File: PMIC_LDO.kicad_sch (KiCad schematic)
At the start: 20 parts, among them U5 RK809-2

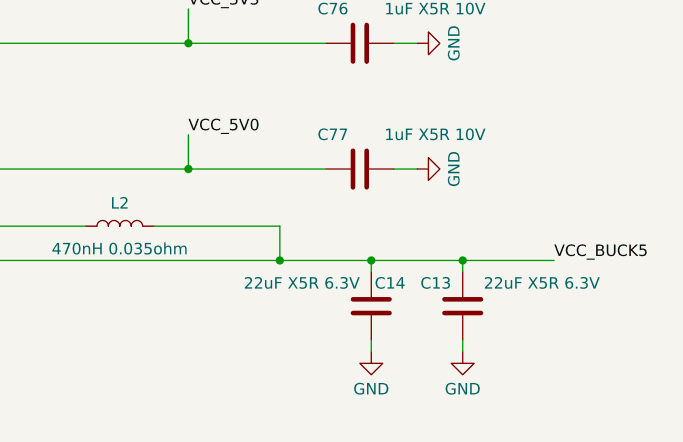
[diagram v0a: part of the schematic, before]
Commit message: updated LCSC selection of capacitors
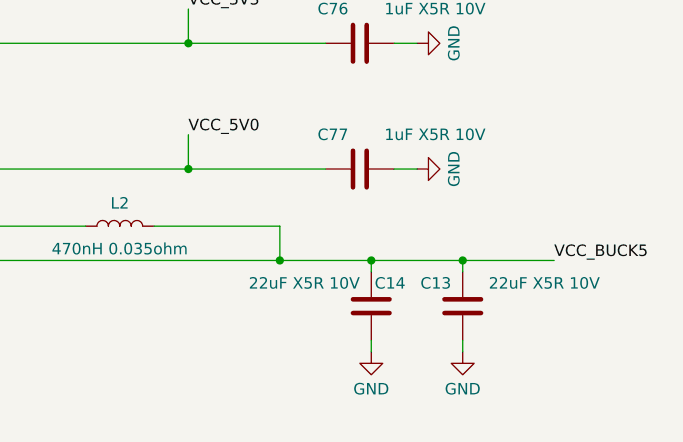
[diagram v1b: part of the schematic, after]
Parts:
- C13, C14: value 22uF X5R 6.3V -> 22uF X5R 10V; LCSC (none) -> C162690; Model (none) -> ZRB18AR61A226ME01L; Vendor (none) -> muRata(村田)
- C66: footprint Capacitor_SMD:C_0603_1608Metric -> Capacitor_SMD:C_0402_1005Metric; LCSC C469532 -> C77000; Model GRM188B31A106KE69D -> GRM155R61A106ME44D
- C67, C68, C69, C71, C72, C73, C74, C75, C76, C77: LCSC (none) -> C77007; Model (none) -> GRM155R61C105KE01D; Vendor (none) -> muRata(村田)
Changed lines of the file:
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@@
+      (effects (font (size 1.27 1.27)) hide)
+    )
+    (property "Description" "容值: 1uF 精度: ±10% 额定电压: 16V 材质(温度系数): X5R 材质:X5R" (at 209.55 118.11 0)
+      (effects (font (size 1.27 1.27)) hide)
+    )
+    (property "LCSC" "C77007" (at 209.55 118.11 0)
+      (effects (font (size 1.27 1.27)) hide)
+    )
+    (property "Model" "GRM155R61C105KE01D" (at 209.55 118.11 0)
+      (effects (font (size 1.27 1.27)) hide)
+    )
+    (property "Vendor" "muRata(村田)" (at 209.55 118.11 0)
       (effects (font (size 1.27 1.27)) hide)
     )
@@
       (effects (font (size 1.27 1.27)) hide)
     )
+    (property "Description" "容值: 1uF 精度: ±10% 额定电压: 16V 材质(温度系数): X5R 材质:X5R" (at 209.55 87.63 0)
+      (effects (font (size 1.27 1.27)) hide)
+    )
+    (property "LCSC" "C77007" (at 209.55 87.63 0)
+      (effects (font (size 1.27 1.27)) hide)
+    )
+    (property "Model" "GRM155R61C105KE01D" (at 209.55 87.63 0)
+      (effects (font (size 1.27 1.27)) hide)
+    )
+    (property "Vendor" "muRata(村田)" (at 209.55 87.63 0)
+      (effects (font (size 1.27 1.27)) hide)
+    )
     (pin "1")
     (pin "2")
@@
       (effects (font (size 1.27 1.27)) hide)
     )
+    (property "Description" "容值: 1uF 精度: ±10% 额定电压: 16V 材质(温度系数): X5R 材质:X5R" (at 209.55 45.72 0)
+      (effects (font (size 1.27 1.27)) hide)
+    )
+    (property "LCSC" "C77007" (at 209.55 45.72 0)
+      (effects (font (size 1.27 1.27)) hide)
+    )
+    (property "Model" "GRM155R61C105KE01D" (at 209.55 45.72 0)
+      (effects (font (size 1.27 1.27)) hide)
+    )
+    (property "Vendor" "muRata(村田)" (at 209.55 45.72 0)
+      (effects (font (size 1.27 1.27)) hide)
+    )
     (pin "1")
     (pin "2")
@@
     )
     (property "Datasheet" "~" (at 209.55 36.83 0)
+      (effects (font (size 1.27 1.27)) hide)
+    )
+    (property "Description" "容值: 1uF 精度: ±10% 额定电压: 16V 材质(温度系数): X5R 材质:X5R" (at 209.55 36.83 0)
+      (effects (font (size 1.27 1.27)) hide)
+    )
+    (property "LCSC" "C77007" (at 209.55 36.83 0)
+      (effects (font (size 1.27 1.27)) hide)
+    )
+    (property "Model" "GRM155R61C105KE01D" (at 209.55 36.83 0)
+      (effects (font (size 1.27 1.27)) hide)
+    )
+    (property "Vendor" "muRata(村田)" (at 209.55 36.83 0)
       (effects (font (size 1.27 1.27)) hide)
     )
@@
       (effects (font (size 1.27 1.27)) hide)
     )
+    (property "Description" "容值: 1uF 精度: ±10% 额定电压: 16V 材质(温度系数): X5R 材质:X5R" (at 209.55 29.21 0)
+      (effects (font (size 1.27 1.27)) hide)
+    )
+    (property "LCSC" "C77007" (at 209.55 29.21 0)
+      (effects (font (size 1.27 1.27)) hide)
+    )
+    (property "Model" "GRM155R61C105KE01D" (at 209.55 29.21 0)
+      (effects (font (size 1.27 1.27)) hide)
+    )
+    (property "Vendor" "muRata(村田)" (at 209.55 29.21 0)
+      (effects (font (size 1.27 1.27)) hide)
+    )
     (pin "1")
     (pin "2")
@@
       (effects (font (size 1.27 1.27)) (justify left))
     )
-    (property "Value" "22uF X5R 6.3V" (at 236.22 144.78 0)
+    (property "Value" "22uF X5R 10V" (at 236.22 144.78 0)
       (effects (font (size 1.27 1.27)) (justify left))
     )
@@
     )
     (property "Datasheet" "~" (at 220.98 147.32 0)
+      (effects (font (size 1.27 1.27)) hide)
+    )
+    (property "Description" "容值: 22uF 精度: ±20% 额定电压: 10V 材质(温度系数): X5R 材质：X5R" (at 220.98 147.32 0)
+      (effects (font (size 1.27 1.27)) hide)
+    )
+    (property "LCSC" "C162690" (at 220.98 147.32 0)
+      (effects (font (size 1.27 1.27)) hide)
+    )
+    (property "Model" "ZRB18AR61A226ME01L" (at 220.98 147.32 0)
+      (effects (font (size 1.27 1.27)) hide)
+    )
+    (property "Vendor" "muRata(村田)" (at 220.98 147.32 0)
       (effects (font (size 1.27 1.27)) hide)
     )
@@
       (effects (font (size 1.27 1.27)) hide)
     )
+    (property "Description" "容值: 1uF 精度: ±10% 额定电压: 16V 材质(温度系数): X5R 材质:X5R" (at 209.55 67.31 0)
+      (effects (font (size 1.27 1.27)) hide)
+    )
+    (property "LCSC" "C77007" (at 209.55 67.31 0)
+      (effects (font (size 1.27 1.27)) hide)
+    )
+    (property "Model" "GRM155R61C105KE01D" (at 209.55 67.31 0)
+      (effects (font (size 1.27 1.27)) hide)
+    )
+    (property "Vendor" "muRata(村田)" (at 209.55 67.31 0)
+      (effects (font (size 1.27 1.27)) hide)
+    )
     (pin "1")
     (pin "2")
@@
       (effects (font (size 1.27 1.27)) hide)
     )
+    (property "Description" "容值: 1uF 精度: ±10% 额定电压: 16V 材质(温度系数): X5R 材质:X5R" (at 209.55 105.41 0)
+      (effects (font (size 1.27 1.27)) hide)
+    )
+    (property "LCSC" "C77007" (at 209.55 105.41 0)
+      (effects (font (size 1.27 1.27)) hide)
+    )
+    (property "Model" "GRM155R61C105KE01D" (at 209.55 105.41 0)
+      (effects (font (size 1.27 1.27)) hide)
+    )
+    (property "Vendor" "muRata(村田)" (at 209.55 105.41 0)
+      (effects (font (size 1.27 1.27)) hide)
+    )
     (pin "1")
     (pin "2")
@@
     )
     (property "Datasheet" "~" (at 209.55 96.52 0)
+      (effects (font (size 1.27 1.27)) hide)
+    )
+    (property "Description" "容值: 1uF 精度: ±10% 额定电压: 16V 材质(温度系数): X5R 材质:X5R" (at 209.55 96.52 0)
+      (effects (font (size 1.27 1.27)) hide)
+    )
+    (property "LCSC" "C77007" (at 209.55 96.52 0)
+      (effects (font (size 1.27 1.27)) hide)
+    )
+    (property "Model" "GRM155R61C105KE01D" (at 209.55 96.52 0)
+      (effects (font (size 1.27 1.27)) hide)
+    )
+    (property "Vendor" "muRata(村田)" (at 209.55 96.52 0)
       (effects (font (size 1.27 1.27)) hide)
     )
@@
       (effects (font (size 1.27 1.27)) hide)
     )
+    (property "Description" "容值: 1uF 精度: ±10% 额定电压: 16V 材质(温度系数): X5R 材质:X5R" (at 209.55 76.2 0)
+      (effects (font (size 1.27 1.27)) hide)
+    )
+    (property "LCSC" "C77007" (at 209.55 76.2 0)
+      (effects (font (size 1.27 1.27)) hide)
+    )
+    (property "Model" "GRM155R61C105KE01D" (at 209.55 76.2 0)
+      (effects (font (size 1.27 1.27)) hide)
+    )
+    (property "Vendor" "muRata(村田)" (at 209.55 76.2 0)
+      (effects (font (size 1.27 1.27)) hide)
+    )
     (pin "1")
     (pin "2")
@@
       (effects (font (size 1.27 1.27)) hide)
     )
+    (property "Description" "容值: 1uF 精度: ±10% 额定电压: 16V 材质(温度系数): X5R 材质:X5R" (at 209.55 132.08 0)
+      (effects (font (size 1.27 1.27)) hide)
+    )
+    (property "LCSC" "C77007" (at 209.55 132.08 0)
+      (effects (font (size 1.27 1.27)) hide)
+    )
+    (property "Model" "GRM155R61C105KE01D" (at 209.55 132.08 0)
+      (effects (font (size 1.27 1.27)) hide)
+    )
+    (property "Vendor" "muRata(村田)" (at 209.55 132.08 0)
+      (effects (font (size 1.27 1.27)) hide)
+    )
     (pin "1")
     (pin "2")
@@
       (effects (font (size 1.27 1.27)) (justify left))
     )
-    (property "Value" "22uF X5R 6.3V" (at 209.55 144.78 0)
+    (property "Value" "22uF X5R 10V" (at 209.55 144.78 0)
       (effects (font (size 1.27 1.27)) (justify left))
     )
@@
     )
     (property "Datasheet" "~" (at 210.82 147.32 0)
+      (effects (font (size 1.27 1.27)) hide)
+    )
+    (property "Description" "容值: 22uF 精度: ±20% 额定电压: 10V 材质(温度系数): X5R 材质：X5R" (at 210.82 147.32 0)
+      (effects (font (size 1.27 1.27)) hide)
+    )
+    (property "LCSC" "C162690" (at 210.82 147.32 0)
+      (effects (font (size 1.27 1.27)) hide)
+    )
+    (property "Model" "ZRB18AR61A226ME01L" (at 210.82 147.32 0)
+      (effects (font (size 1.27 1.27)) hide)
+    )
+    (property "Vendor" "muRata(村田)" (at 210.82 147.32 0)
       (effects (font (size 1.27 1.27)) hide)
     )
@@
       (effects (font (size 1.27 1.27)) (justify left))
     )
-    (property "Footprint" "Capacitor_SMD:C_0603_1608Metric" (at 111.4552 152.4 0)
+    (property "Footprint" "Capacitor_SMD:C_0402_1005Metric" (at 111.4552 152.4 0)
       (effects (font (size 1.27 1.27)) hide)
     )
@@
       (effects (font (size 1.27 1.27)) hide)
     )
-    (property "Description" "容值: 10uF 精度: ±10% 额定电压: 10V 材质(温度系数): B B(JIS)" (at 110.49 148.59 0)
-      (effects (font (size 1.27 1.27)) hide)
-    )
-    (property "LCSC" "C469532" (at 110.49 148.59 0)
-      (effects (font (size 1.27 1.27)) hide)
-    )
-    (property "Model" "GRM188B31A106KE69D" (at 110.49 148.59 0)
-      (effects (font (size 1.27 1.27)) hide)
-    )
+    (property "Description" "容值: 10uF 精度: ±20% 额定电压: 10V 材质(温度系数): X5R 材质:X5R" (at 110.49 148.59 0)
+      (effects (font (size 1.27 1.27)) hide)
+    )
+    (property "LCSC" "C77000" (at 110.49 148.59 0)
+      (effects (font (size 1.27 1.27)) hide)
+    )
+    (property "Model" "GRM155R61A106ME44D" (at 110.49 148.59 0)
+      (effects (font (size 1.27 1.27)) hide)
+    )

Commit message: updated foorprints
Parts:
- L2: value 470nH 0.035ohm -> 470nH 4.53A 0.035ohm; footprint (none) -> Inductor_SMD:L_1008_2520Metric; LCSC (none) -> C88530; Model (none) -> VLS252010HBX-R47M-1; Vendor (none) -> TDK
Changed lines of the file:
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@@
       (effects (font (size 1.27 1.27)))
     )
-    (property "Value" "470nH 0.035ohm" (at 182.88 140.97 90)
+    (property "Value" "470nH 4.53A 0.035ohm" (at 182.88 140.97 90)
       (effects (font (size 1.27 1.27)))
     )
-    (property "Footprint" "" (at 182.88 138.43 0)
+    (property "Footprint" "Inductor_SMD:L_1008_2520Metric" (at 182.88 138.43 0)
       (effects (font (size 1.27 1.27)) hide)
     )
@@
       (effects (font (size 1.27 1.27)) hide)
     )
+    (property "Description" "电感值: 470nH 精度: ±20% 额定电流: 3.32A 饱和电流(Isat): 4.53A 直流电阻(DCR): 35mΩ Q值: - 自谐振频率: - 车" (at 182.88 138.43 0)
+      (effects (font (size 1.27 1.27)) hide)
+    )
+    (property "LCSC" "C88530" (at 182.88 138.43 0)
+      (effects (font (size 1.27 1.27)) hide)
+    )
+    (property "Model" "VLS252010HBX-R47M-1" (at 182.88 138.43 0)
+      (effects (font (size 1.27 1.27)) hide)
+    )
+    (property "Vendor" "TDK" (at 182.88 138.43 0)
+      (effects (font (size 1.27 1.27)) hide)
+    )

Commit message: layout SoC Power and DDR capacitors
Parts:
- C62, C63, C64, C65: footprint Capacitor_SMD:C_0201_0603Metric -> Capacitor_SMD:C_0402_1005Metric; LCSC C76929 -> C15684; Model GRM033R60J105KEA2D -> GRM155R60J105KE19D
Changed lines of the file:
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@@
       (effects (font (size 1.27 1.27)) (justify left))
     )
-    (property "Footprint" "Capacitor_SMD:C_0201_0603Metric" (at 111.4552 127 0)
+    (property "Footprint" "Capacitor_SMD:C_0402_1005Metric" (at 111.4552 127 0)
       (effects (font (size 1.27 1.27)) hide)
     )
@@
       (effects (font (size 1.27 1.27)) hide)
     )
-    (property "LCSC" "C76929" (at 110.49 123.19 0)
-      (effects (font (size 1.27 1.27)) hide)
-    )
-    (property "Model" "GRM033R60J105KEA2D" (at 110.49 123.19 0)
+    (property "LCSC" "C15684" (at 110.49 123.19 0)
+      (effects (font (size 1.27 1.27)) hide)
+    )
+    (property "Model" "GRM155R60J105KE19D" (at 110.49 123.19 0)
       (effects (font (size 1.27 1.27)) hide)
     )
@@
       (effects (font (size 1.27 1.27)) (justify left))
     )
-    (property "Footprint" "Capacitor_SMD:C_0201_0603Metric" (at 111.4552 40.64 0)
+    (property "Footprint" "Capacitor_SMD:C_0402_1005Metric" (at 111.4552 40.64 0)
       (effects (font (size 1.27 1.27)) hide)
     )
@@
       (effects (font (size 1.27 1.27)) hide)
     )
-    (property "LCSC" "C76929" (at 110.49 36.83 0)
-      (effects (font (size 1.27 1.27)) hide)
-    )
-    (property "Model" "GRM033R60J105KEA2D" (at 110.49 36.83 0)
+    (property "LCSC" "C15684" (at 110.49 36.83 0)
+      (effects (font (size 1.27 1.27)) hide)
+    )
+    (property "Model" "GRM155R60J105KE19D" (at 110.49 36.83 0)
       (effects (font (size 1.27 1.27)) hide)
     )
@@
       (effects (font (size 1.27 1.27)) (justify left))
     )
-    (property "Footprint" "Capacitor_SMD:C_0201_0603Metric" (at 111.4552 68.58 0)
+    (property "Footprint" "Capacitor_SMD:C_0402_1005Metric" (at 111.4552 68.58 0)
       (effects (font (size 1.27 1.27)) hide)
     )
@@
       (effects (font (size 1.27 1.27)) hide)
     )
-    (property "LCSC" "C76929" (at 110.49 64.77 0)
-      (effects (font (size 1.27 1.27)) hide)
-    )
-    (property "Model" "GRM033R60J105KEA2D" (at 110.49 64.77 0)
+    (property "LCSC" "C15684" (at 110.49 64.77 0)
+      (effects (font (size 1.27 1.27)) hide)
+    )
+    (property "Model" "GRM155R60J105KE19D" (at 110.49 64.77 0)
       (effects (font (size 1.27 1.27)) hide)
     )
@@
       (effects (font (size 1.27 1.27)) (justify left))
     )
-    (property "Footprint" "Capacitor_SMD:C_0201_0603Metric" (at 111.4552 99.06 0)
+    (property "Footprint" "Capacitor_SMD:C_0402_1005Metric" (at 111.4552 99.06 0)
       (effects (font (size 1.27 1.27)) hide)
     )
@@
       (effects (font (size 1.27 1.27)) hide)
     )
-    (property "LCSC" "C76929" (at 110.49 95.25 0)
-      (effects (font (size 1.27 1.27)) hide)
-    )
-    (property "Model" "GRM033R60J105KEA2D" (at 110.49 95.25 0)
-      (effects (font (size 1.27 1.27)) hide)
-    )
+    (property "LCSC" "C15684" (at 110.49 95.25 0)
+      (effects (font (size 1.27 1.27)) hide)
+    )
+    (property "Model" "GRM155R60J105KE19D" (at 110.49 95.25 0)
+      (effects (font (size 1.27 1.27)) hide)
+    )

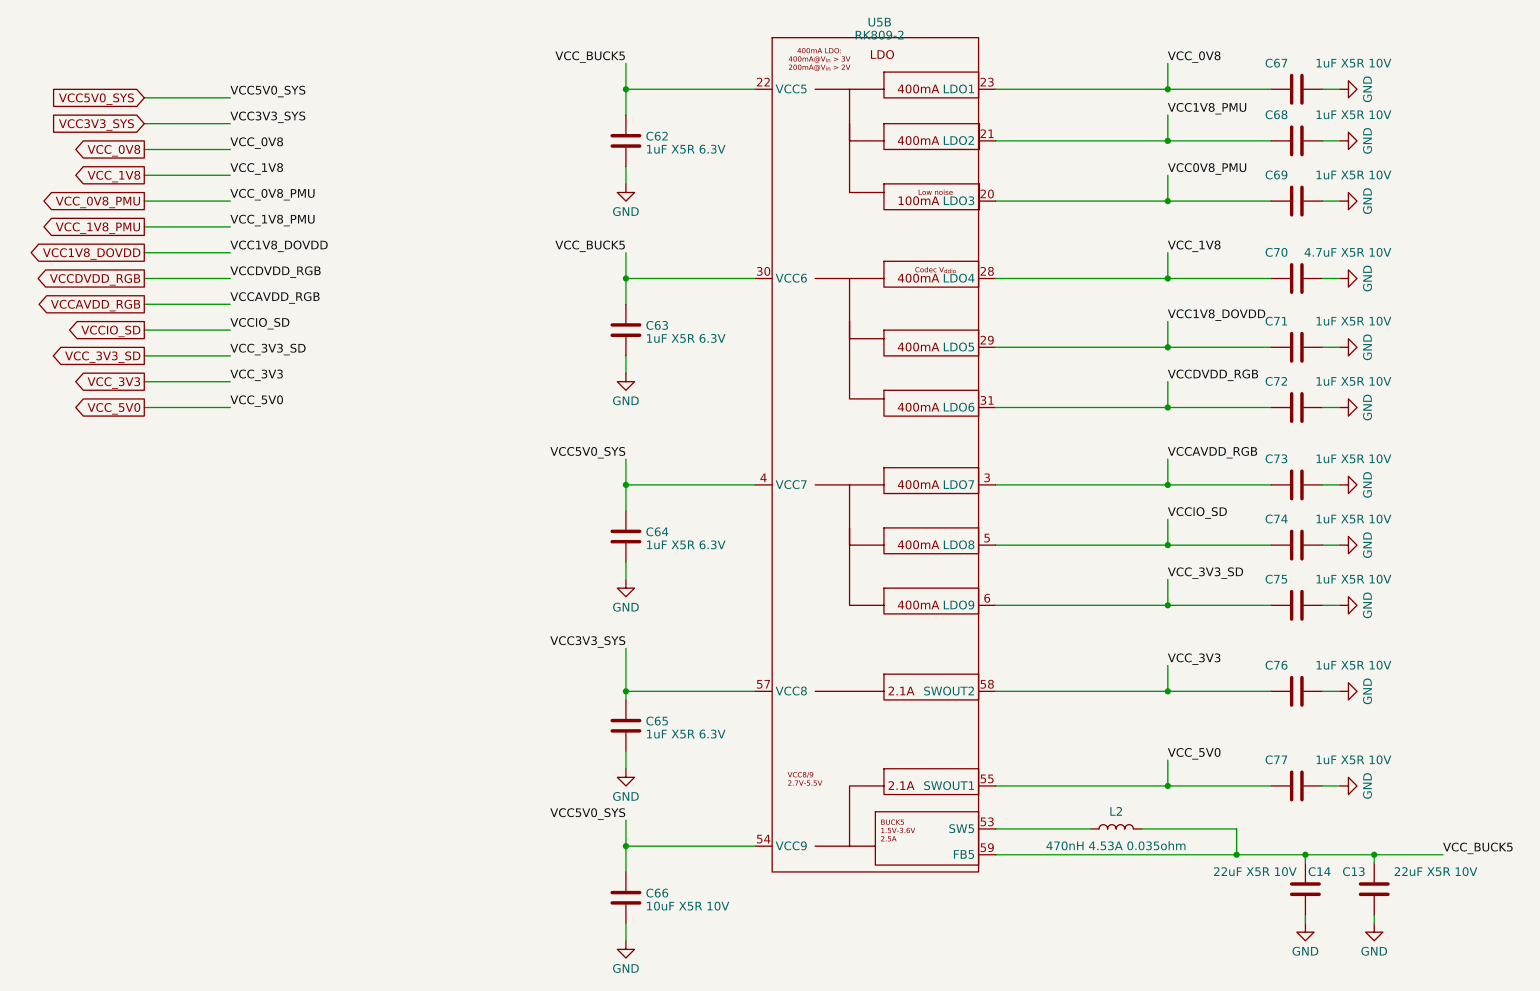
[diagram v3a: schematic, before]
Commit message: fix some ERCs
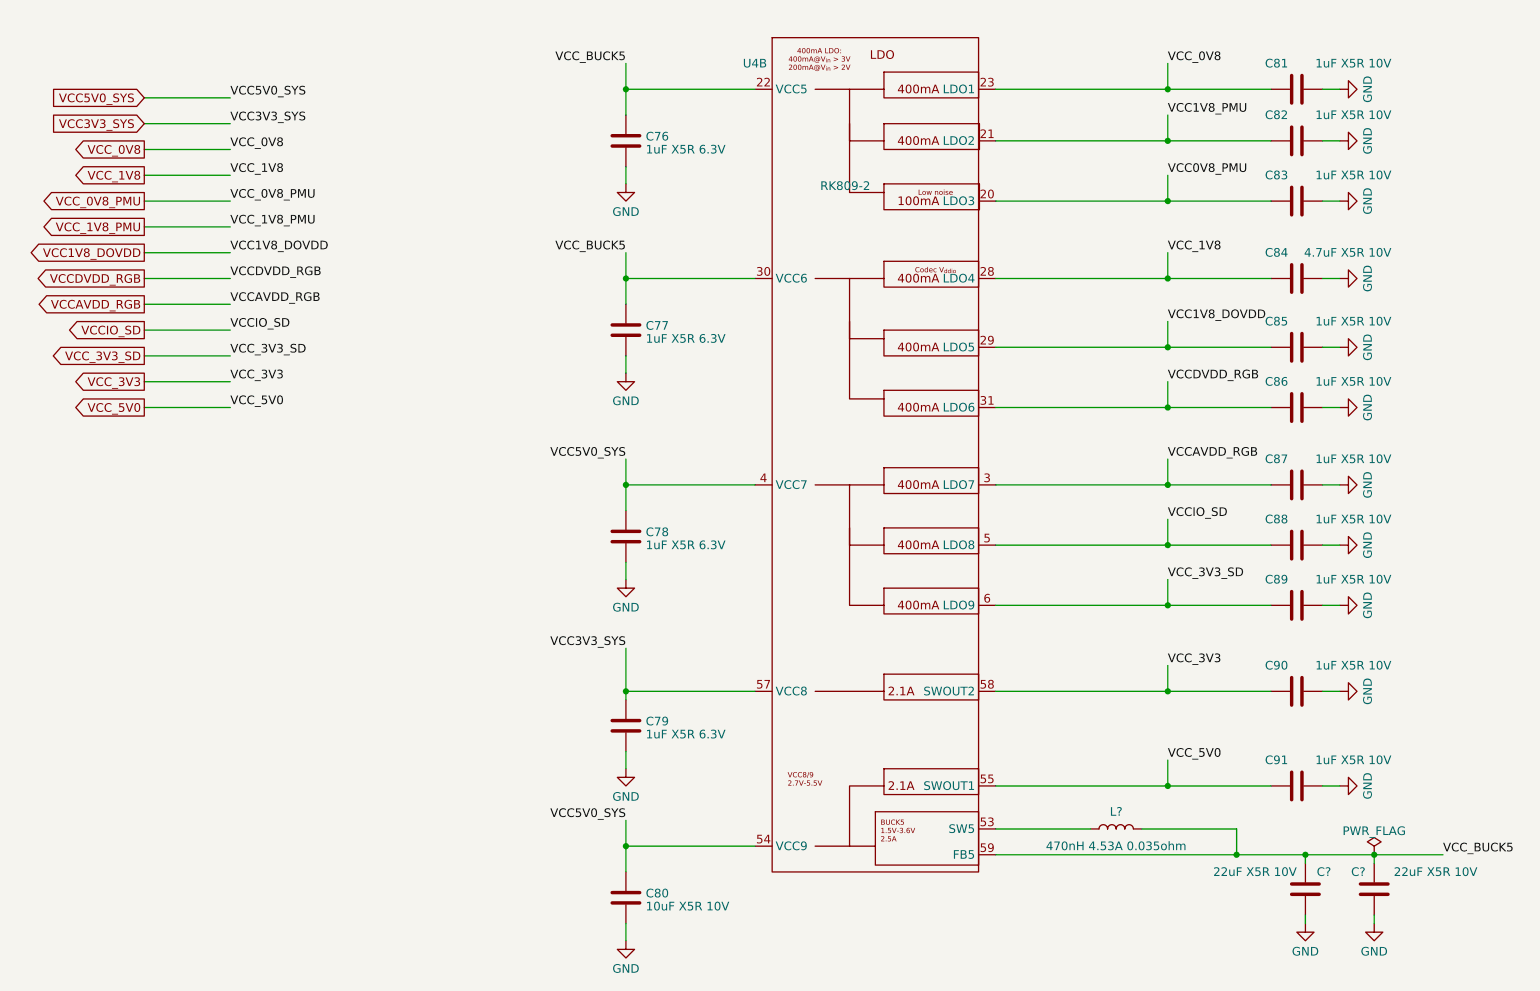
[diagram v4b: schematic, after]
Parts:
- renumbered C62 to C76, C63 to C77, C64 to C78, C65 to C79, C66 to C80, C67 to C81, C68 to C82, C69 to C83, C70 to C84, C71 to C85, C72 to C86, C73 to C87, C74 to C88, C75 to C89, C76 to C90, C77 to C91, C13 to C?, C14 to C?, L2 to L?, U5 to U4

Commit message: added VDD Logic
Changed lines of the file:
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@@
+    (stroke (width 0) (type default))
+  )
+  (wire (pts (xy 39.37 82.55) (xy 52.07 82.55))
     (stroke (width 0) (type default))
   )
@@
   )
   (label "VCC1V8_DOVDD" (at 52.07 53.34 0) (fields_autoplaced)
+    (effects (font (size 1.27 1.27)) (justify left bottom))
+  )
+  (label "VCC_BUCK5" (at 52.07 82.55 0) (fields_autoplaced)
     (effects (font (size 1.27 1.27)) (justify left bottom))
   )
@@
       (effects (font (size 1.27 1.27)) (justify right) hide)
     )
+  )
+  (global_label "VCC_BUCK5" (shape output) (at 39.37 82.55 180) (fields_autoplaced)
+    (effects (font (size 1.27 1.27)) (justify right))
+    (property "Intersheetrefs" "${INTERSHEET_REFS}" (at 25.518 82.55 0)
+      (effects (font (size 1.27 1.27)) (justify right) hide)
+    )

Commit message: fix ERC
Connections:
- net VCC0V8_PMU is gone; now on net VCC_0V8_PMU: C83.1, U4.20 (LDO3)
- net VCC1V8_PMU is gone; now on net VCC_1V8_PMU: C82.1, U4.21 (LDO2)
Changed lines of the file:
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@@
     (effects (font (size 1.27 1.27)) (justify left bottom))
   )
-  (label "VCC0V8_PMU" (at 190.5 41.91 0) (fields_autoplaced)
+  (label "VCC_0V8_PMU" (at 190.5 41.91 0) (fields_autoplaced)
     (effects (font (size 1.27 1.27)) (justify left bottom))
   )
-  (label "VCC1V8_PMU" (at 190.5 33.02 0) (fields_autoplaced)
+  (label "VCC_1V8_PMU" (at 190.5 33.02 0) (fields_autoplaced)
     (effects (font (size 1.27 1.27)) (justify left bottom))
   )

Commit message: added OSC, updated annotations
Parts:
- renumbered C76 to C15001, C77 to C15002, C78 to C15003, C79 to C15004, C80 to C15005, C81 to C15006, C82 to C15007, C83 to C15008, C84 to C15009, C85 to C15010, C86 to C15011, C87 to C15012, C88 to C15013, C89 to C15014, C90 to C15015, C91 to C15016, U4 to U13001
